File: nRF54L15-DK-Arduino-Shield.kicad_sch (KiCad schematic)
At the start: 15 parts

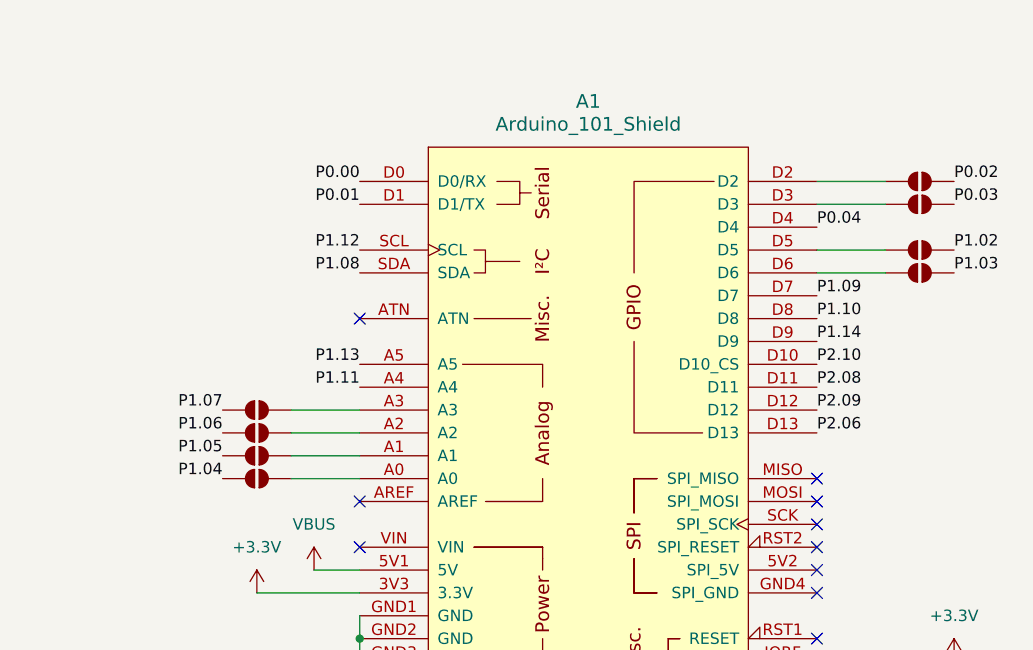
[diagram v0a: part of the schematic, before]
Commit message: Updates for LR1110 Arduino shield
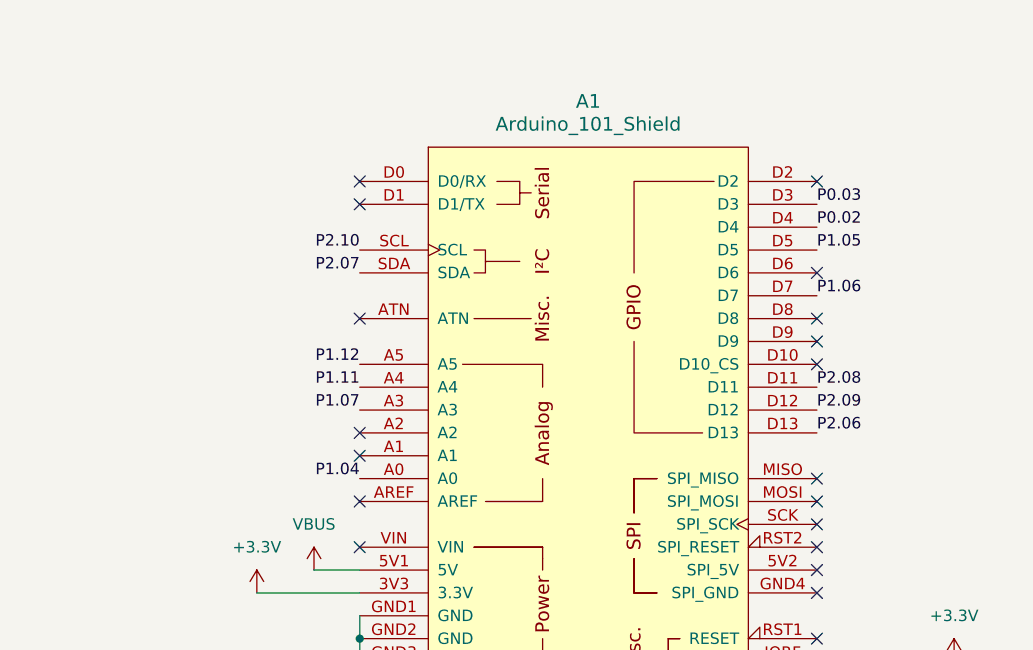
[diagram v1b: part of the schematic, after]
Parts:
- removed JP1, JP2, JP3, JP4, JP5, JP6, JP7, JP8: SolderJumper_2_Open, Jumper:SolderJumper-2_P1.3mm_Open_RoundedPad1.0x1.5mm, symbol Jumper:SolderJumper_2_Open
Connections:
- net P0.00: no longer A1.D0 (D0/RX)
- net P0.01: no longer A1.D1 (D1/TX)
- net P0.02: now also A1.D4
- net P0.03: now also A1.D3
- net P0.04: no longer A1.D4
- net P1.04: now also A1.A0
- net P1.05: now also A1.D5
- net P1.06: now also A1.D7
- net P1.07: now also A1.A3
- net P1.08: no longer A1.SDA
- net P1.09: no longer A1.D7
- net P1.10: no longer A1.D8
- net P1.12: now also A1.A5; no longer A1.SCL
- net P1.13: no longer A1.A5
- net P1.14: no longer A1.D9
- net P2.07: now also A1.SDA
- net P2.10: now also A1.SCL; no longer A1.D10 (D10_CS)
- no-connect marks 37 -> 46

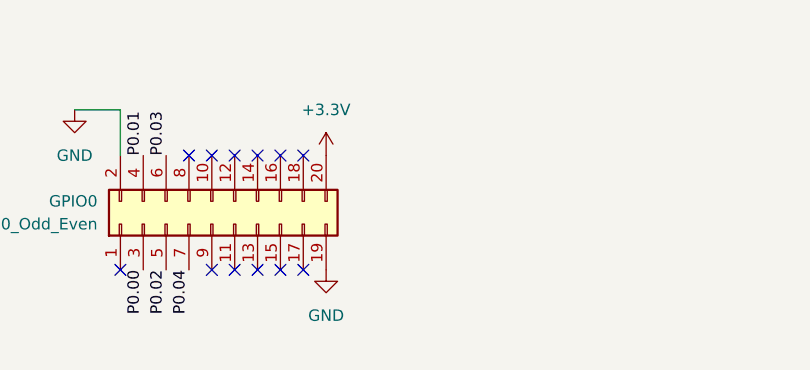
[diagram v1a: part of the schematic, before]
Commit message: Added VDD jumper
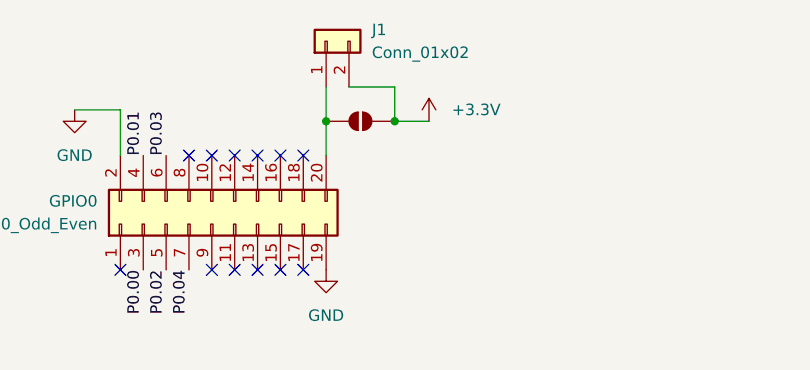
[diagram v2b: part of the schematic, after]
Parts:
- added J1: Conn_01x02, Connector_PinHeader_2.54mm:PinHeader_1x02_P2.54mm_Vertical, symbol Connector_Generic:Conn_01x02
- added JP1: SolderJumper_2_Open, Jumper:SolderJumper-2_P1.3mm_Open_RoundedPad1.0x1.5mm, symbol Jumper:SolderJumper_2_Open
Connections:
- net +3.3V: now also J1.2 (Pin_2), JP1.2 (B); no longer GPIO0.20 (Pin_20)
- new net: GPIO0.20 (Pin_20), J1.1 (Pin_1), JP1.1 (A)
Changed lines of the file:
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@@
 	(paper "A4")
+	(junction
+		(at 115.57 50.8)
+		(diameter 0)
+		(color 0 0 0 0)
+	)
 	(junction
 		(at 193.04 119.38)
@@
 	)
 	(junction
+		(at 107.95 50.8)
+		(diameter 0)
+		(color 0 0 0 0)
+	)
+	(junction
 		(at 29.21 91.44)
 		(diameter 0)
@@
 	(wire
 		(pts
-			(xy 243.84 119.38) (xy 259.08 119.38)
+			(xy 115.57 50.8) (xy 119.38 50.8)
 		)
 		(stroke
@@
 	(wire
 		(pts
-			(xy 85.09 87.63) (xy 85.09 91.44)
+			(xy 243.84 119.38) (xy 259.08 119.38)
 		)
 		(stroke
@@
 	(wire
 		(pts
-			(xy 187.96 109.22) (xy 193.04 109.22)
+			(xy 85.09 87.63) (xy 85.09 91.44)
 		)
 		(stroke
@@
 	(wire
 		(pts
-			(xy 80.01 49.53) (xy 85.09 49.53)
+			(xy 187.96 109.22) (xy 193.04 109.22)
 		)
 		(stroke
@@
 	(wire
 		(pts
-			(xy 29.21 54.61) (xy 31.75 54.61)
+			(xy 107.95 50.8) (xy 107.95 54.61)
 		)
 		(stroke
@@
 	(wire
 		(pts
-			(xy 81.28 123.19) (xy 85.09 123.19)
+			(xy 80.01 49.53) (xy 85.09 49.53)
 		)
 		(stroke
@@
 	(wire
 		(pts
-			(xy 20.32 127) (xy 30.48 127)
+			(xy 29.21 54.61) (xy 31.75 54.61)
 		)
 		(stroke
@@
 	(wire
 		(pts
-			(xy 81.28 87.63) (xy 85.09 87.63)
+			(xy 81.28 123.19) (xy 85.09 123.19)
 		)
 		(stroke
@@
 	(wire
 		(pts
-			(xy 29.21 91.44) (xy 31.75 91.44)
+			(xy 20.32 127) (xy 30.48 127)
 		)
 		(stroke
@@
 	(wire
 		(pts
-			(xy 85.09 49.53) (xy 85.09 54.61)
+			(xy 81.28 87.63) (xy 85.09 87.63)
 		)
 		(stroke
@@
 	(wire
 		(pts
-			(xy 30.48 127) (xy 33.02 127)
+			(xy 29.21 91.44) (xy 31.75 91.44)
 		)
 		(stroke
@@
 	(wire
 		(pts
-			(xy 19.05 67.31) (xy 29.21 67.31)
+			(xy 115.57 46.99) (xy 115.57 50.8)
 		)
 		(stroke
@@
 	(wire
 		(pts
-			(xy 19.05 91.44) (xy 29.21 91.44)
+			(xy 85.09 49.53) (xy 85.09 54.61)
 		)
 		(stroke
@@
 	(wire
 		(pts
+			(xy 30.48 127) (xy 33.02 127)
+		)
+		(stroke
+			(width 0)
+			(type default)
+		)
+	)
+	(wire
+		(pts
+			(xy 107.95 46.99) (xy 107.95 50.8)
+		)
+		(stroke
+			(width 0)
+			(type default)
+		)
+	)
+	(wire
+		(pts
+			(xy 19.05 67.31) (xy 29.21 67.31)
+		)
+		(stroke
+			(width 0)
+			(type default)
+		)
+	)
+	(wire
+		(pts
+			(xy 19.05 91.44) (xy 29.21 91.44)
+		)
+		(stroke
+			(width 0)
+			(type default)
+		)
+	)
+	(wire
+		(pts
 			(xy 193.04 116.84) (xy 193.04 119.38)
+		)
+		(stroke
+			(width 0)
+			(type default)
+		)
+	)
+	(wire
+		(pts
+			(xy 110.49 46.99) (xy 115.57 46.99)
 		)
 		(stroke
@@
 	)
 	(symbol
+		(lib_id "Jumper:SolderJumper_2_Open")
+		(at 111.76 50.8 0)
+		(unit 1)
+		(exclude_from_sim no)
+		(in_bom no)
+		(on_board yes)
+		(dnp no)
+		(fields_autoplaced yes)
+		(property "Reference" "JP1"
+			(at 111.76 44.45 0)
+			(effects
+				(font
+					(size 1.27 1.27)
+				)
+				(hide yes)
+			)
+		)
+		(property "Value" "SolderJumper_2_Open"
+			(at 111.76 46.99 0)
+			(effects
+				(font
+					(size 1.27 1.27)
+				)
+				(hide yes)
+			)
+		)
+		(property "Footprint" "Jumper:SolderJumper-2_P1.3mm_Open_RoundedPad1.0x1.5mm"
+			(at 111.76 50.8 0)
+			(effects
+				(font
+					(size 1.27 1.27)
+				)
+				(hide yes)
+			)
+		)
+		(property "Datasheet" "~"
+			(at 111.76 50.8 0)
+			(effects
+				(font
+					(size 1.27 1.27)
+				)
+				(hide yes)
+			)
+		)
+		(property "Description" "Solder Jumper, 2-pole, open"
+			(at 111.76 50.8 0)
+			(effects
+				(font
+					(size 1.27 1.27)
+				)
+				(hide yes)
+			)
+		)
+		(pin "1"
+		)
+		(pin "2"
+		)
+		(instances
+			(project ""
+				(path "/cab962bd-2af5-48c0-b36b-f604681d0ad9"
+					(reference "JP1")
+					(unit 1)
+				)
+			)
+		)
+	)
+	(symbol
 		(lib_id "power:GND")
 		(at 193.04 119.38 0)
@@
 	(symbol
 		(lib_id "power:+3.3V")
-		(at 107.95 54.61 0)
+		(at 119.38 50.8 0)
 		(unit 1)
 		(exclude_from_sim no)
@@
 		(fields_autoplaced yes)
 		(property "Reference" "#PWR020"
-			(at 107.95 58.42 0)
+			(at 119.38 54.61 0)
 			(effects
 				(font
@@
 		)
 		(property "Value" "+3.3V"
-			(at 107.95 49.53 0)
-			(effects
-				(font
-					(size 1.27 1.27)
-				)
+			(at 121.92 49.5299 0)
+			(effects
+				(font
+					(size 1.27 1.27)
+				)
+				(justify left)
 			)
 		)
 		(property "Footprint" ""
-			(at 107.95 54.61 0)
+			(at 119.38 50.8 0)
 			(effects
 				(font
@@
 		)
 		(property "Datasheet" ""
-			(at 107.95 54.61 0)
+			(at 119.38 50.8 0)
 			(effects
 				(font
@@
 		)
 		(property "Description" "Power symbol creates a global label with name \"+3.3V\""
-			(at 107.95 54.61 0)
+			(at 119.38 50.8 0)
 			(effects
 				(font
@@
 					(unit 1)
 				)
+			)
+		)
+	)
+	(symbol
+		(lib_id "Connector_Generic:Conn_01x02")
+		(at 107.95 41.91 90)
+		(unit 1)
+		(exclude_from_sim no)
+		(in_bom yes)
+		(on_board yes)
+		(dnp no)
+		(fields_autoplaced yes)
+		(property "Reference" "J1"
+			(at 113.03 40.6399 90)
+			(effects
+				(font
+					(size 1.27 1.27)
+				)
+				(justify right)
+			)
+		)
+		(property "Value" "Conn_01x02"
+			(at 113.03 43.1799 90)
+			(effects
+				(font
+					(size 1.27 1.27)
+				)
+				(justify right)
+			)
+		)
+		(property "Footprint" "Connector_PinHeader_2.54mm:PinHeader_1x02_P2.54mm_Vertical"
+			(at 107.95 41.91 0)
+			(effects
+				(font
+					(size 1.27 1.27)
+				)
+				(hide yes)
+			)
+		)
+		(property "Datasheet" "~"
+			(at 107.95 41.91 0)
+			(effects
+				(font
+					(size 1.27 1.27)
+				)
+				(hide yes)
+			)
+		)
+		(property "Description" "Generic connector, single row, 01x02, script generated (kicad-library-utils/schlib/autogen/connector/)"
+			(at 107.95 41.91 0)
+			(effects
+				(font
+					(size 1.27 1.27)
+				)
+				(hide yes)
+			)
+		)
+		(pin "2"
+		)
+		(pin "1"
+		)
+		(instances
+			(project ""
+				(path "/cab962bd-2af5-48c0-b36b-f604681d0ad9"
+					(reference "J1")
+					(unit 1)
+				)
